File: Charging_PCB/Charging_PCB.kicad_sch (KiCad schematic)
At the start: 56 parts, among them K101 Relay_SPDT_Omron_G2RL-1, K102 Relay_SPDT_Omron_G2RL-1, Q1 NMOS, Q101 Q_PMOS_GSD, Q102 Q_PMOS_GSD, Q103 Q_NPN_BEC, Q104 Q_NPN_BEC, Q105 Q_NPN_BEC, Q106 Q_NPN_BEC, Q107 Q_PMOS_GSD, Q108 Q_PMOS_GSD, Q2 NMOS, SW101 SW_Omron_B3FS, SW102 SW_Omron_B3FS, U1 SFH617A-1, U101 641964-1, U102 641964-1, U103 641964-1, U107 LM7805_TO220, U2 SFH617A-1, U3 74AHC1G00, U4 74AHC1G00, U5 74LS279

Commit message: Added SR Latch to charging PCB, completed gerbers,bom,and CPL file and added mouser parts list to assembly file
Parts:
- K101, K102: JLC# C1524507 -> C469130
- U1, U2, U5: now not fitted
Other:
- moved on the sheet: H101, H102, H103, H104
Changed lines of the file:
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@@
 	(text_box "Mounting Holes"
 		(exclude_from_sim no)
-		(at 147.32 154.94 0)
+		(at 295.91 165.1 0)
 		(size 49.53 21.59)
 		(margins 0.9525 0.9525 0.9525 0.9525)
@@
 		(in_bom yes)
 		(on_board yes)
-		(dnp no)
+		(dnp yes)
 		(fields_autoplaced yes)
 		(property "Reference" "U5"
@@
 	(symbol
 		(lib_id "Mechanical:MountingHole")
-		(at 175.26 170.18 0)
+		(at 323.85 180.34 0)
 		(unit 1)
 		(exclude_from_sim yes)
@@
 		(fields_autoplaced yes)
 		(property "Reference" "H104"
-			(at 177.8 168.9099 0)
+			(at 326.39 179.0699 0)
 			(effects
 				(font
@@
 		)
 		(property "Value" "MountingHole"
-			(at 177.8 171.4499 0)
+			(at 326.39 181.6099 0)
 			(effects
 				(font
@@
 		)
 		(property "Footprint" "MountingHole:MountingHole_3.2mm_M3"
-			(at 175.26 170.18 0)
+			(at 323.85 180.34 0)
 			(effects
 				(font
@@
 		)
 		(property "Datasheet" "~"
-			(at 175.26 170.18 0)
+			(at 323.85 180.34 0)
 			(effects
 				(font
@@
 		)
 		(property "Description" "Mounting Hole without connection"
-			(at 175.26 170.18 0)
+			(at 323.85 180.34 0)
 			(effects
 				(font
@@
 		)
 		(property "Notes" ""
-			(at 175.26 170.18 0)
+			(at 323.85 180.34 0)
 			(effects
 				(font
@@
 					(size 1.27 1.27)
 				)
-				(hide yes)
 			)
 		)
@@
 			)
 		)
-		(property "JLC#" "C1524507"
+		(property "JLC#" " C469130"
 			(at 96.52 119.38 90)
 			(effects
@@
 	(symbol
 		(lib_id "Mechanical:MountingHole")
-		(at 175.26 161.29 0)
+		(at 323.85 171.45 0)
 		(unit 1)
 		(exclude_from_sim yes)
@@
 		(fields_autoplaced yes)
 		(property "Reference" "H103"
-			(at 177.8 160.0199 0)
+			(at 326.39 170.1799 0)
 			(effects
 				(font
@@
 		)
 		(property "Value" "MountingHole"
-			(at 177.8 162.5599 0)
+			(at 326.39 172.7199 0)
 			(effects
 				(font
@@
 		)
 		(property "Footprint" "MountingHole:MountingHole_3.2mm_M3"
-			(at 175.26 161.29 0)
+			(at 323.85 171.45 0)
 			(effects
 				(font
@@
 		)
 		(property "Datasheet" "~"
-			(at 175.26 161.29 0)
+			(at 323.85 171.45 0)
 			(effects
 				(font
@@
 		)
 		(property "Description" "Mounting Hole without connection"
-			(at 175.26 161.29 0)
+			(at 323.85 171.45 0)
 			(effects
 				(font
@@
 		)
 		(property "Notes" ""
-			(at 175.26 161.29 0)
+			(at 323.85 171.45 0)
 			(effects
 				(font
@@
 					(size 1.27 1.27)
 				)
-				(hide yes)
 			)
 		)
@@
 			)
 		)
-		(property "JLC#" "C1524507"
+		(property "JLC#" " C469130"
 			(at 320.04 129.54 0)
 			(effects
@@
 			)
 		)
-		(property "Datasheet" "641964-1"
+		(property "Datasheet" "https://www.mouser.com/datasheet/2/418/9/ENG_CS_82181_SOFTSHELL_STANDARD_DENSITY_0508-3353168.pdf"
 			(at 29.21 173.99 0)
 			(effects
@@
 		(in_bom yes)
 		(on_board yes)
-		(dnp no)
+		(dnp yes)
 		(fields_autoplaced yes)
 		(property "Reference" "U5"
@@
 		(in_bom yes)
 		(on_board yes)
-		(dnp no)
+		(dnp yes)
 		(fields_autoplaced yes)
 		(property "Reference" "U5"
@@
 	(symbol
 		(lib_id "Mechanical:MountingHole")
-		(at 153.67 170.18 0)
+		(at 302.26 180.34 0)
 		(unit 1)
 		(exclude_from_sim yes)
@@
 		(fields_autoplaced yes)
 		(property "Reference" "H102"
-			(at 156.21 168.9099 0)
+			(at 304.8 179.0699 0)
 			(effects
 				(font
@@
 		)
 		(property "Value" "MountingHole"
-			(at 156.21 171.4499 0)
+			(at 304.8 181.6099 0)
 			(effects
 				(font
@@
 		)
 		(property "Footprint" "MountingHole:MountingHole_3.2mm_M3"
-			(at 153.67 170.18 0)
+			(at 302.26 180.34 0)
 			(effects
 				(font
@@
 		)
 		(property "Datasheet" "~"
-			(at 153.67 170.18 0)
+			(at 302.26 180.34 0)
 			(effects
 				(font
@@
 		)
 		(property "Description" "Mounting Hole without connection"
-			(at 153.67 170.18 0)
+			(at 302.26 180.34 0)
 			(effects
 				(font
@@
 		)
 		(property "Notes" ""
-			(at 153.67 170.18 0)
+			(at 302.26 180.34 0)
 			(effects
 				(font
@@
 		(in_bom yes)
 		(on_board yes)
-		(dnp no)
+		(dnp yes)
 		(fields_autoplaced yes)
 		(property "Reference" "U5"
@@
 		(in_bom yes)
 		(on_board yes)
-		(dnp no)
+		(dnp yes)
 		(property "Reference" "U2"
 			(at 387.35 85.598 0)
@@
 	(symbol
 		(lib_id "Mechanical:MountingHole")
-		(at 153.67 161.29 0)
+		(at 302.26 171.45 0)
 		(unit 1)
 		(exclude_from_sim yes)
@@
 		(fields_autoplaced yes)
 		(property "Reference" "H101"
-			(at 156.21 160.0199 0)
+			(at 304.8 170.1799 0)
 			(effects
 				(font
@@
 		)
 		(property "Value" "MountingHole"
-			(at 156.21 162.5599 0)
+			(at 304.8 172.7199 0)
 			(effects
 				(font
@@
 		)
 		(property "Footprint" "MountingHole:MountingHole_3.2mm_M3"
-			(at 153.67 161.29 0)
+			(at 302.26 171.45 0)
 			(effects
 				(font
@@
 		)
 		(property "Datasheet" "~"
-			(at 153.67 161.29 0)
+			(at 302.26 171.45 0)
 			(effects
 				(font
@@
 		)
 		(property "Description" "Mounting Hole without connection"
-			(at 153.67 161.29 0)
+			(at 302.26 171.45 0)
 			(effects
 				(font
@@
 		)
 		(property "Notes" ""
-			(at 153.67 161.29 0)
+			(at 302.26 171.45 0)
 			(effects
 				(font
@@
 		(in_bom yes)
 		(on_board yes)
-		(dnp no)
+		(dnp yes)
 		(property "Reference" "U1"
 			(at 185.42 86.614 0)
@@
 		(in_bom yes)
 		(on_board yes)
-		(dnp no)
+		(dnp yes)
 		(fields_autoplaced yes)
 		(property "Reference" "U5"

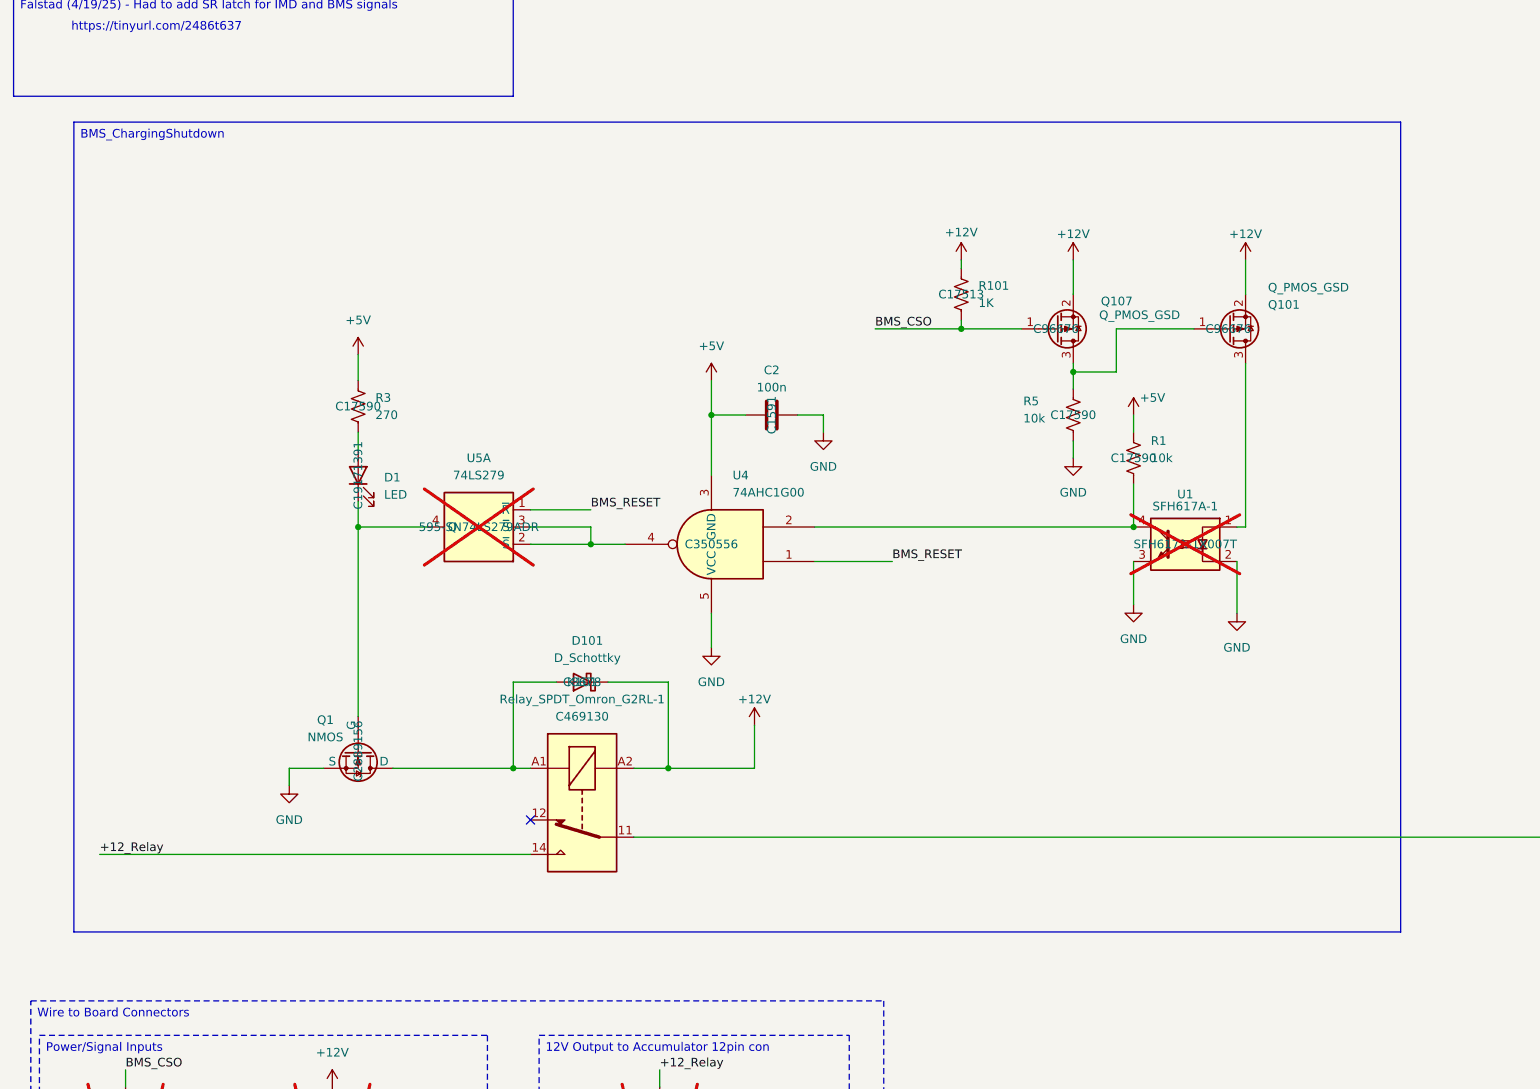
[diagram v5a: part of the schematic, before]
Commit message: ESF documentation and wiring schematics for charging
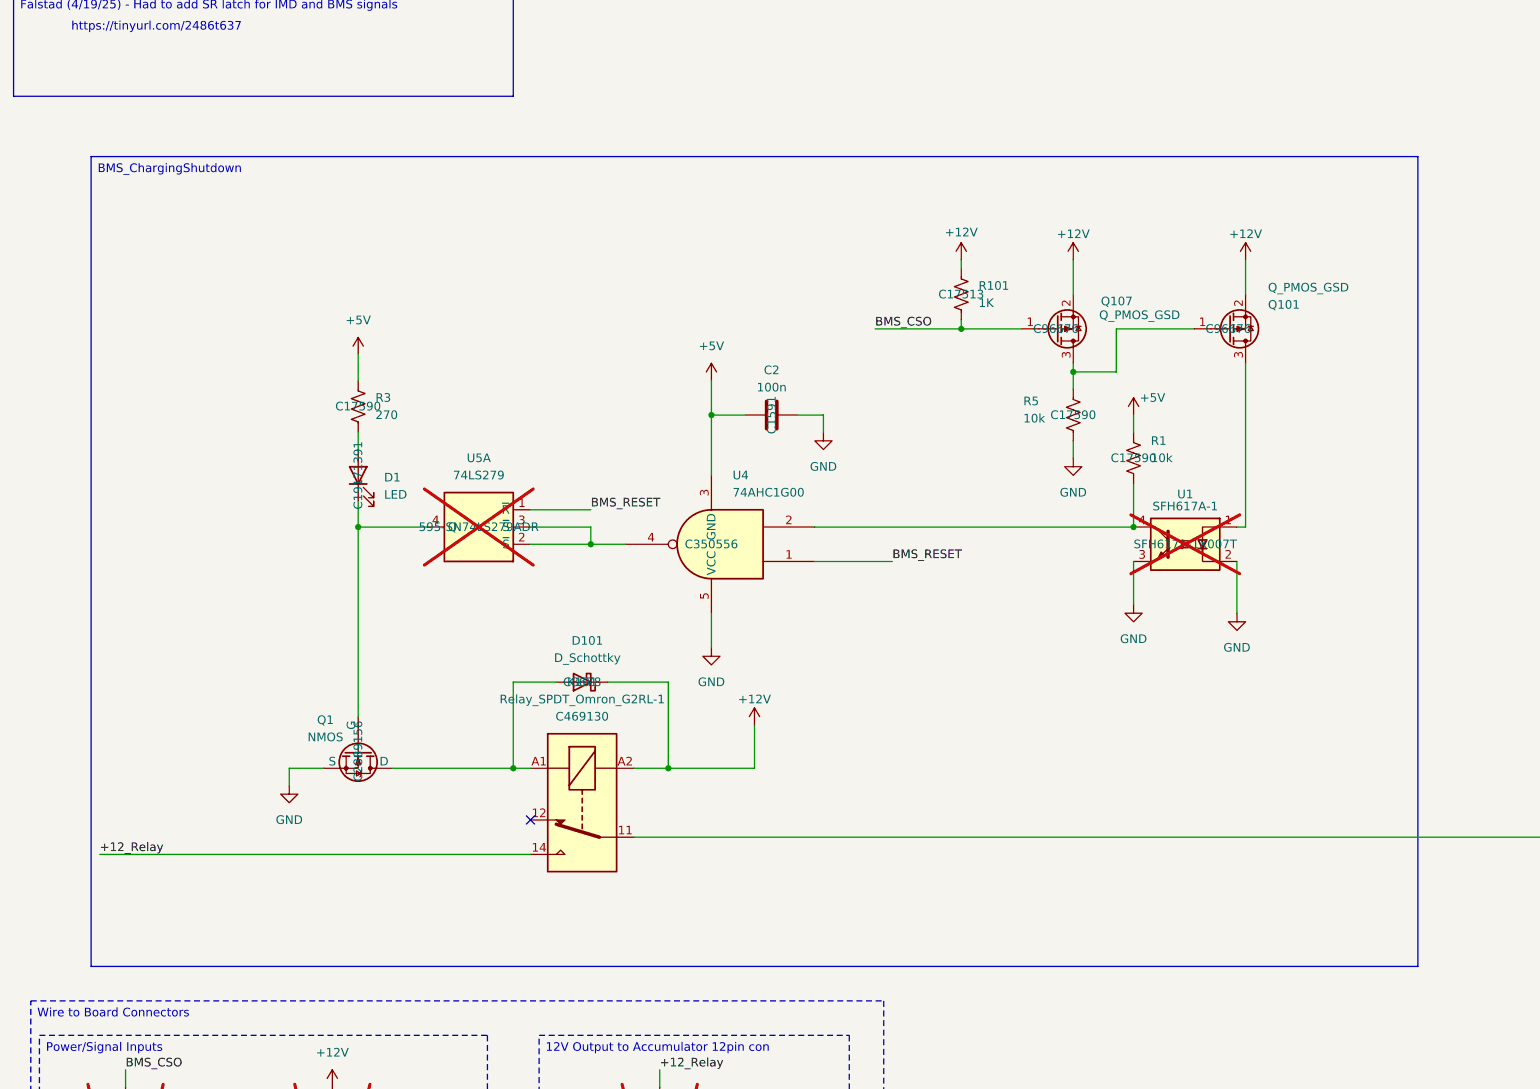
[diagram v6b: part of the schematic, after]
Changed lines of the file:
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@@
 	(text_box "BMS_ChargingShutdown"
 		(exclude_from_sim no)
-		(at 21.59 31.75 0)
+		(at 24.13 36.83 0)
 		(size 195.58 119.38)
 		(margins 0.9525 0.9525 0.9525 0.9525)
